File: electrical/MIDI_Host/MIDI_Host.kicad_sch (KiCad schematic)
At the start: 6 parts, among them CN1 USB-CON-AF-LCP-Offset, J1 Blackheadphonejack, J2 Blackheadphonejack, J3 USB_C_TYPE-C-32-M-12, SW1 ST-0-102-C03-N003-RS

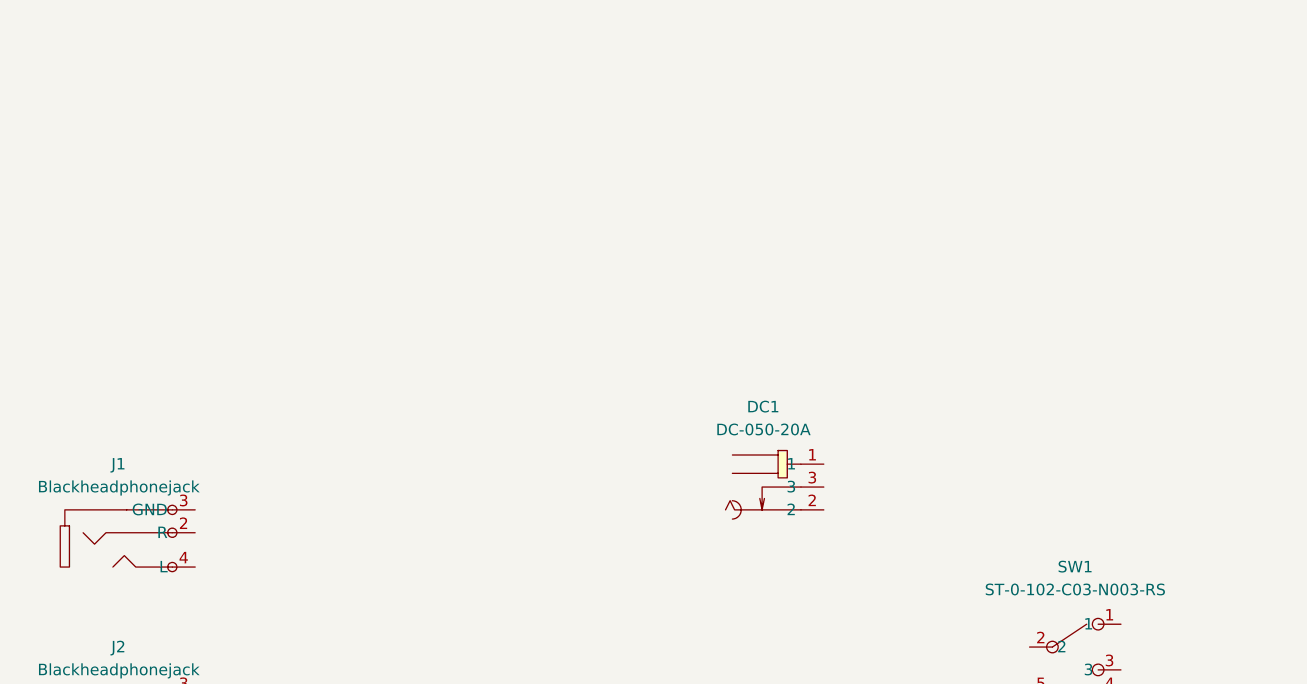
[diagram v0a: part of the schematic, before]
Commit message: SUKU host devboard created, cicd added
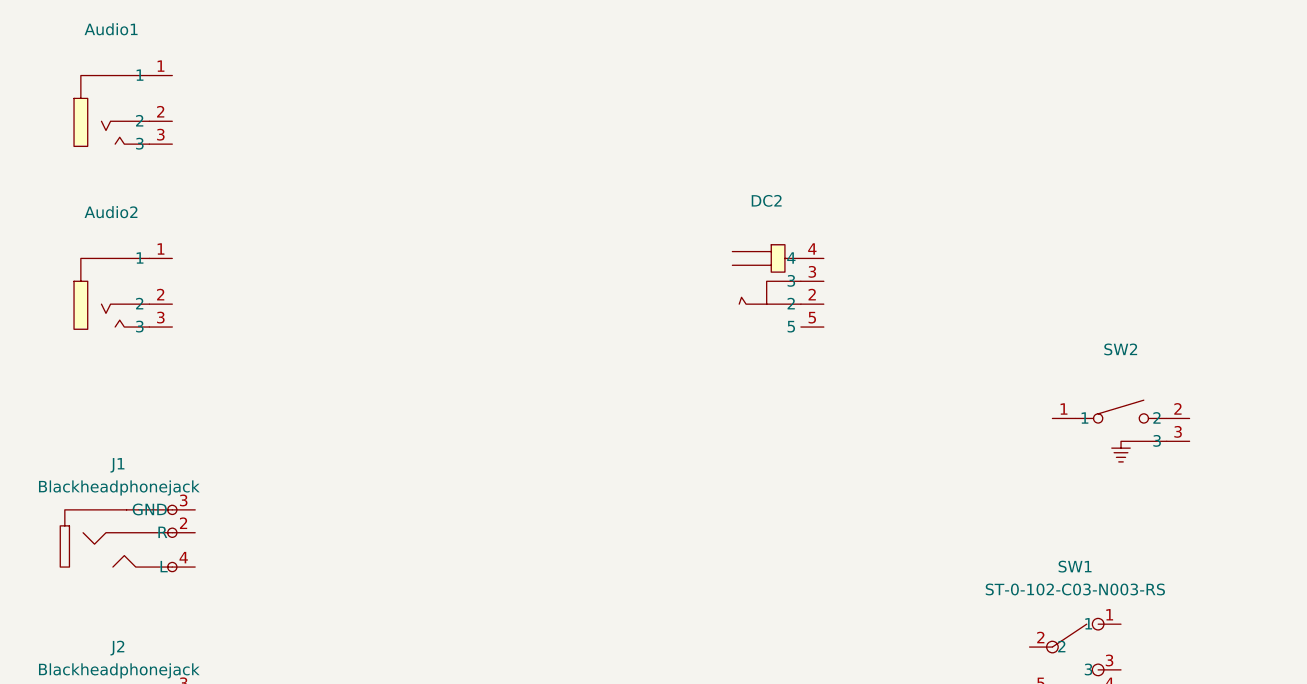
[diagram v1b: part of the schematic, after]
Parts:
- removed DC1: DC-050-20A, suku_basics:DC-IN-SMD_DC-050-20A, symbol suku_basics:DC-050-20A
- added Audio1, Audio2: (no value), symbol suku_basics:PJ-320B
- added DC2: (no value), symbol suku_basics:DC-C033D-5.5A-2.5
- added SW2: (no value), symbol suku_basics:TC-1109DE-C-G
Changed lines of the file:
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@@
     (pin "S4")
+  )
+  (symbol (lib_id "suku_basics:DC-C033D-5.5A-2.5") (at 139.7 38.1 0) (unit 1)
+    (in_bom yes) (on_board yes) (fields_autoplaced)
+    (property "Reference" "DC2" (id 0) (at 135.89 29.21 0))
+    (property "Value" "" (id 1) (at 135.89 31.75 0))
+    (property "Footprint" "" (id 2) (at 139.7 50.8 0)
+      (effects (font (size 1.27 1.27)) hide)
+    )
+    (property "Datasheet" "https://lcsc.com/product-detail/Power-Connectors_XKB-Enterprise-DC-C033D-5-5A-2-5_C397336.html" (id 3) (at 139.7 53.34 0)
+      (effects (font (size 1.27 1.27)) hide)
+    )
+    (property "Manufacturer" "XKB Enterprise" (id 4) (at 139.7 55.88 0)
+      (effects (font (size 1.27 1.27)) hide)
+    )
+    (property "LCSC Part" "C397336" (id 5) (at 139.7 58.42 0)
+      (effects (font (size 1.27 1.27)) hide)
+    )
+    (pin "2")
+    (pin "3")
+    (pin "4")
+    (pin "5")
   )
   (symbol (lib_id "suku_basics:Blackheadphonejack") (at 66.04 66.04 0) (unit 1)
@@
     (pin "5")
   )
+  (symbol (lib_id "suku_basics:PJ-320B") (at 66.04 38.1 0) (unit 1)
+    (in_bom yes) (on_board yes) (fields_autoplaced)
+    (property "Reference" "Audio2" (id 0) (at 63.12 30.48 0))
+    (property "Value" "" (id 1) (at 63.12 33.02 0))
+    (property "Footprint" "" (id 2) (at 66.04 50.8 0)
+      (effects (font (size 1.27 1.27)) hide)
+    )
+    (property "Datasheet" "https://lcsc.com/product-detail/Audio-Connectors_3-5mmCloth-headphone-jack_C18594.html" (id 3) (at 66.04 53.34 0)
+      (effects (font (size 1.27 1.27)) hide)
+    )
+    (property "Manufacturer" "BOOMELE" (id 4) (at 66.04 55.88 0)
+      (effects (font (size 1.27 1.27)) hide)
+    )
+    (property "LCSC Part" "C18594" (id 5) (at 66.04 58.42 0)
+      (effects (font (size 1.27 1.27)) hide)
+    )
+    (property "JLC Part" "Extended Part" (id 6) (at 66.04 60.96 0)
+      (effects (font (size 1.27 1.27)) hide)
+    )
+    (pin "1")
+    (pin "2")
+    (pin "3")
+  )
+  (symbol (lib_id "suku_basics:PJ-320B") (at 66.04 17.78 0) (unit 1)
+    (in_bom yes) (on_board yes) (fields_autoplaced)
+    (property "Reference" "Audio1" (id 0) (at 63.12 10.16 0))
+    (property "Value" "" (id 1) (at 63.12 12.7 0))
+    (property "Footprint" "" (id 2) (at 66.04 30.48 0)
+      (effects (font (size 1.27 1.27)) hide)
+    )
+    (property "Datasheet" "https://lcsc.com/product-detail/Audio-Connectors_3-5mmCloth-headphone-jack_C18594.html" (id 3) (at 66.04 33.02 0)
+      (effects (font (size 1.27 1.27)) hide)
+    )
+    (property "Manufacturer" "BOOMELE" (id 4) (at 66.04 35.56 0)
+      (effects (font (size 1.27 1.27)) hide)
+    )
+    (property "LCSC Part" "C18594" (id 5) (at 66.04 38.1 0)
+      (effects (font (size 1.27 1.27)) hide)
+    )
+    (property "JLC Part" "Extended Part" (id 6) (at 66.04 40.64 0)
+      (effects (font (size 1.27 1.27)) hide)
+    )
+    (pin "1")
+    (pin "2")
+    (pin "3")
+  )
+  (symbol (lib_id "suku_basics:TC-1109DE-C-G") (at 175.26 53.34 0) (unit 1)
+    (in_bom yes) (on_board yes) (fields_autoplaced)
+    (property "Reference" "SW2" (id 0) (at 175.26 45.72 0))
+    (property "Value" "" (id 1) (at 175.26 48.26 0))
+    (property "Footprint" "" (id 2) (at 175.26 63.5 0)
+      (effects (font (size 1.27 1.27)) hide)
+    )
+    (property "Datasheet" "https://lcsc.com/product-detail/Tactile-Switches_XKB-Enterprise-TC-1109DE-C-G_C400325.html" (id 3) (at 175.26 66.04 0)
+      (effects (font (size 1.27 1.27)) hide)
+    )
+    (property "Manufacturer" "XKB Enterprise" (id 4) (at 175.26 68.58 0)
+      (effects (font (size 1.27 1.27)) hide)
+    )
+    (property "LCSC Part" "C400325" (id 5) (at 175.26 71.12 0)
+      (effects (font (size 1.27 1.27)) hide)
+    )
+    (property "JLC Part" "Extended Part" (id 6) (at 175.26 73.66 0)
+      (effects (font (size 1.27 1.27)) hide)
+    )
+    (pin "1")
+    (pin "2")
+    (pin "3")
+  )
   (symbol (lib_id "suku_basics:Blackheadphonejack") (at 66.04 86.36 0) (unit 1)
     (in_bom yes) (on_board yes) (fields_autoplaced)
@@
     (pin "SH2")
   )
-  (symbol (lib_id "suku_basics:DC-050-20A") (at 139.7 60.96 0) (unit 1)
-    (in_bom yes) (on_board yes) (fields_autoplaced)
-    (property "Reference" "DC1" (id 0) (at 135.51 52.07 0))
-    (property "Value" "DC-050-20A" (id 1) (at 135.51 54.61 0))
-    (property "Footprint" "suku_basics:DC-IN-SMD_DC-050-20A" (id 2) (at 139.7 71.12 0)
-      (effects (font (size 1.27 1.27)) hide)
-    )
-    (property "Datasheet" "" (id 3) (at 139.7 60.96 0)
-      (effects (font (size 1.27 1.27)) hide)
-    )
-    (property "Manufacturer" "韩国韩荣" (id 4) (at 139.7 73.66 0)
-      (effects (font (size 1.27 1.27)) hide)
-    )
-    (property "LCSC Part" "C707276" (id 5) (at 139.7 76.2 0)
-      (effects (font (size 1.27 1.27)) hide)
-    )
-    (property "JLC Part" "Extended Part" (id 6) (at 139.7 78.74 0)
-      (effects (font (size 1.27 1.27)) hide)
-    )
-    (pin "1")
-    (pin "2")
-    (pin "3")
-  )
   (sheet_instances
     (path "/" (page "1"))
   )
   (symbol_instances
+    (path "/b58d647c-1ae7-4d06-97c8-66cde03fb16a"
+      (reference "Audio1") (unit 1) (value "PJ-320B") (footprint "suku_basics:AUDIO-SMD_PJ-320B")
+    )
+    (path "/a62f3716-14a3-419d-9103-6b6e5d48dea5"
+      (reference "Audio2") (unit 1) (value "PJ-320B") (footprint "suku_basics:AUDIO-SMD_PJ-320B")
+    )
     (path "/cc7fdda4-1f0b-4447-b8f5-2a7f9266383d"
       (reference "CN1") (unit 1) (value "USB-CON-AF-LCP-Offset") (footprint "suku_basics:USB-A-SMD_AF-LCP-OFFSET")
     )
-    (path "/da0518d1-a4a1-4d96-a115-d0b555fd0563"
-      (reference "DC1") (unit 1) (value "DC-050-20A") (footprint "suku_basics:DC-IN-SMD_DC-050-20A")
+    (path "/3ebfe238-c44b-4b15-bdba-ea713a53a98c"
+      (reference "DC2") (unit 1) (value "DC-C033D-5.5A-2.5") (footprint "suku_basics:DC-IN-TH_DC-C033D-5.5A-2.5")
     )
     (path "/450fd788-d806-48b1-a032-8afdc8273e6e"
@@
       (reference "SW1") (unit 1) (value "ST-0-102-C03-N003-RS") (footprint "suku_basics:SW-TH_ST-0-102-C03-N003-RS")
     )
-  )
+    (path "/be6da077-d179-463a-af26-1bac671e85bf"
+      (reference "SW2") (unit 1) (value "TC-1109DE-C-G") (footprint "suku_basics:SW-TH_3P-L4.5-W7.0-P3.00-LS1.9")
+    )
+  )

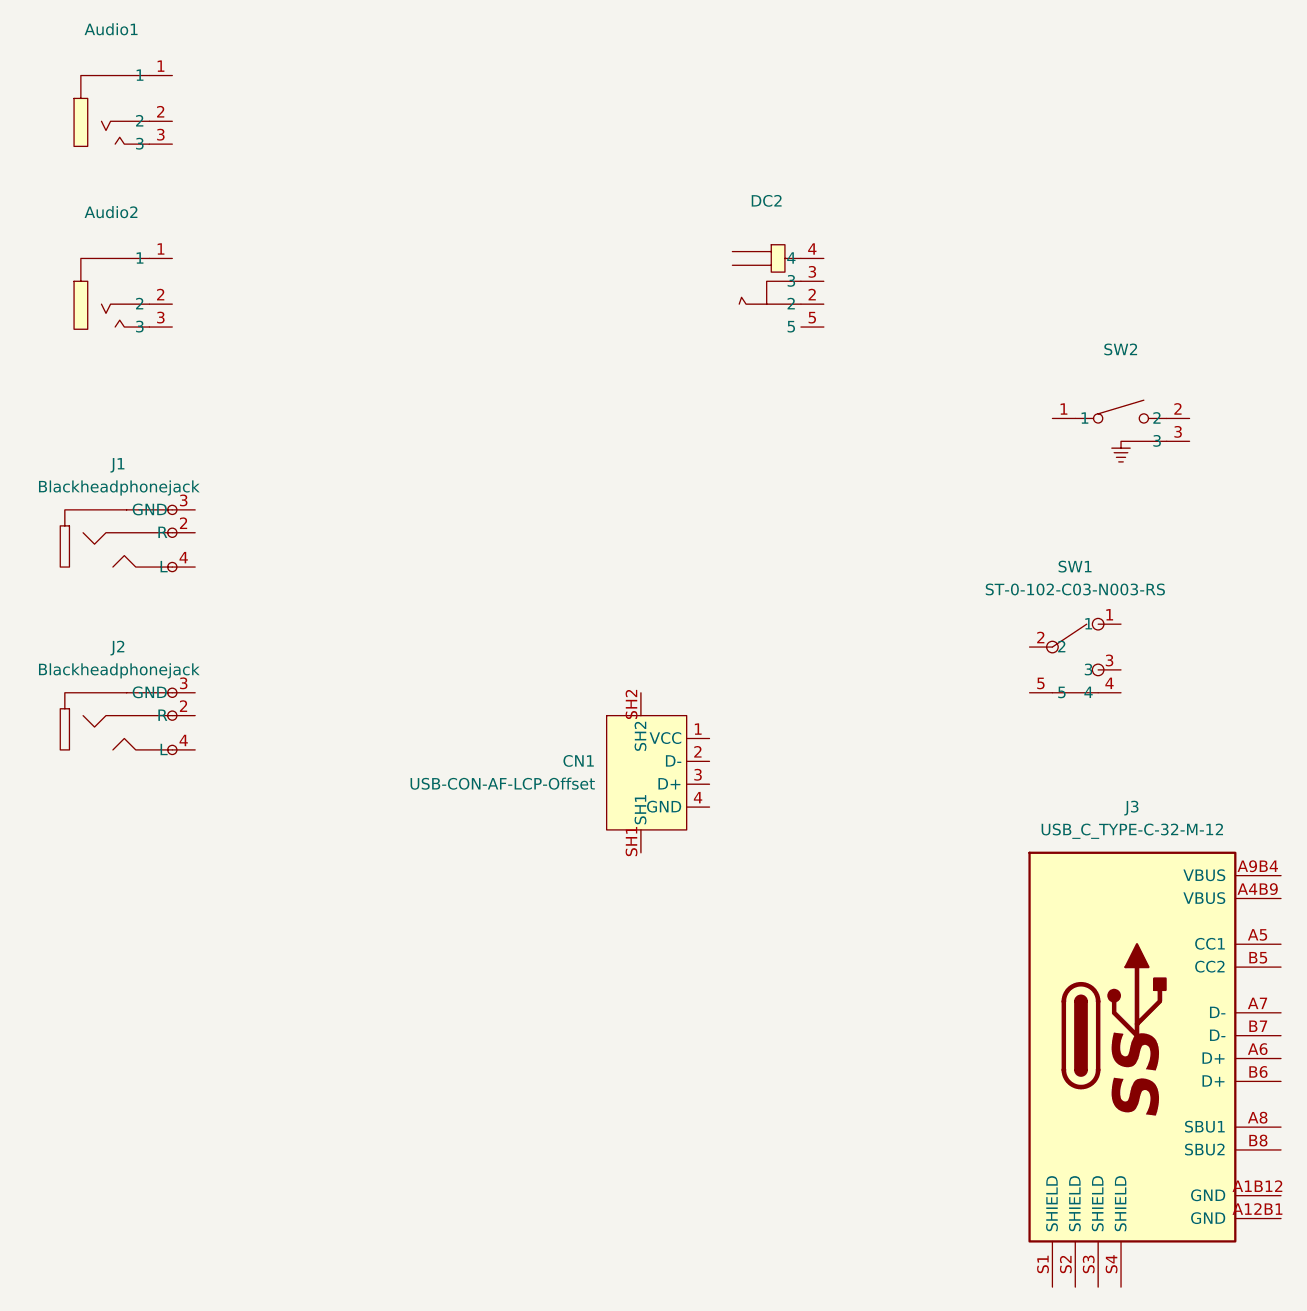
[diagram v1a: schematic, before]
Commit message: SUKU nc flags added to unused pins
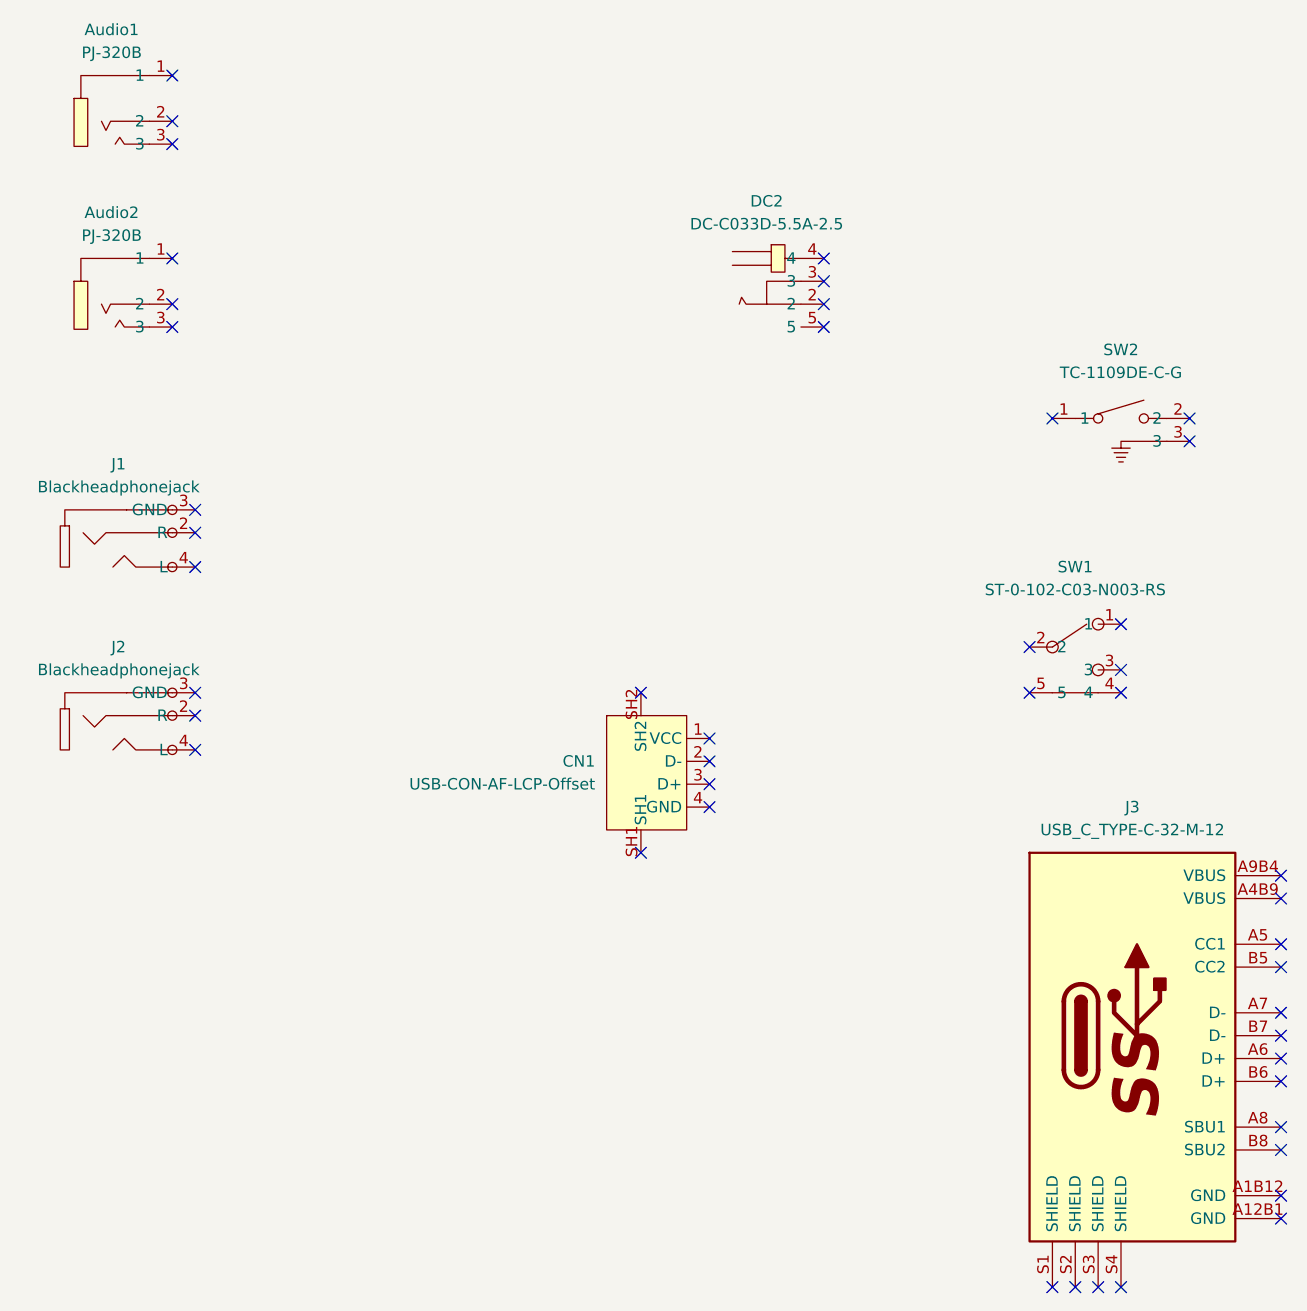
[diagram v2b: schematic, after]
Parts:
- Audio1, Audio2: value (none) -> PJ-320B; footprint (none) -> suku_basics:AUDIO-SMD_PJ-320B
- DC2: value (none) -> DC-C033D-5.5A-2.5; footprint (none) -> suku_basics:DC-IN-TH_DC-C033D-5.5A-2.5
- SW2: value (none) -> TC-1109DE-C-G; footprint (none) -> suku_basics:SW-TH_3P-L4.5-W7.0-P3.00-LS1.9
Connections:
- no-connect marks 0 -> 46
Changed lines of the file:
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@@
 (kicad_sch (version 20211123) (generator eeschema)
   (paper "A4")
+  (no_connect (at 142.24 35.56))
+  (no_connect (at 142.24 38.1))
+  (no_connect (at 142.24 40.64))
+  (no_connect (at 142.24 43.18))
+  (no_connect (at 72.39 83.82))
+  (no_connect (at 72.39 90.17))
+  (no_connect (at 72.39 86.36))
+  (no_connect (at 129.54 88.9))
+  (no_connect (at 129.54 91.44))
+  (no_connect (at 129.54 93.98))
+  (no_connect (at 121.92 101.6))
+  (no_connect (at 121.92 83.82))
+  (no_connect (at 129.54 96.52))
+  (no_connect (at 165.1 78.74))
+  (no_connect (at 165.1 83.82))
+  (no_connect (at 175.26 83.82))
+  (no_connect (at 193.04 104.14))
+  (no_connect (at 182.88 53.34))
+  (no_connect (at 182.88 55.88))
+  (no_connect (at 167.64 53.34))
+  (no_connect (at 175.26 81.28))
+  (no_connect (at 175.26 76.2))
+  (no_connect (at 167.64 149.86))
+  (no_connect (at 170.18 149.86))
+  (no_connect (at 172.72 149.86))
+  (no_connect (at 175.26 149.86))
+  (no_connect (at 193.04 142.24))
+  (no_connect (at 193.04 139.7))
+  (no_connect (at 193.04 134.62))
+  (no_connect (at 193.04 132.08))
+  (no_connect (at 193.04 127))
+  (no_connect (at 193.04 124.46))
+  (no_connect (at 193.04 121.92))
+  (no_connect (at 193.04 119.38))
+  (no_connect (at 193.04 114.3))
+  (no_connect (at 193.04 111.76))
+  (no_connect (at 193.04 106.68))
+  (no_connect (at 69.85 15.24))
+  (no_connect (at 69.85 20.32))
+  (no_connect (at 69.85 22.86))
+  (no_connect (at 69.85 40.64))
+  (no_connect (at 72.39 69.85))
+  (no_connect (at 72.39 66.04))
+  (no_connect (at 69.85 35.56))
+  (no_connect (at 69.85 43.18))
+  (no_connect (at 72.39 63.5))
   (symbol (lib_id "suku_basics:USB_C_TYPE-C-32-M-12") (at 177.8 121.92 0) (unit 1)
     (in_bom yes) (on_board yes) (fields_autoplaced)
@@
     (in_bom yes) (on_board yes) (fields_autoplaced)
     (property "Reference" "DC2" (id 0) (at 135.89 29.21 0))
-    (property "Value" "" (id 1) (at 135.89 31.75 0))
-    (property "Footprint" "" (id 2) (at 139.7 50.8 0)
+    (property "Value" "DC-C033D-5.5A-2.5" (id 1) (at 135.89 31.75 0))
+    (property "Footprint" "suku_basics:DC-IN-TH_DC-C033D-5.5A-2.5" (id 2) (at 139.7 50.8 0)
       (effects (font (size 1.27 1.27)) hide)
     )
@@
     (in_bom yes) (on_board yes) (fields_autoplaced)
     (property "Reference" "Audio2" (id 0) (at 63.12 30.48 0))
-    (property "Value" "" (id 1) (at 63.12 33.02 0))
-    (property "Footprint" "" (id 2) (at 66.04 50.8 0)
+    (property "Value" "PJ-320B" (id 1) (at 63.12 33.02 0))
+    (property "Footprint" "suku_basics:AUDIO-SMD_PJ-320B" (id 2) (at 66.04 50.8 0)
       (effects (font (size 1.27 1.27)) hide)
     )
@@
     (in_bom yes) (on_board yes) (fields_autoplaced)
     (property "Reference" "Audio1" (id 0) (at 63.12 10.16 0))
-    (property "Value" "" (id 1) (at 63.12 12.7 0))
-    (property "Footprint" "" (id 2) (at 66.04 30.48 0)
+    (property "Value" "PJ-320B" (id 1) (at 63.12 12.7 0))
+    (property "Footprint" "suku_basics:AUDIO-SMD_PJ-320B" (id 2) (at 66.04 30.48 0)
       (effects (font (size 1.27 1.27)) hide)
     )
@@
     (in_bom yes) (on_board yes) (fields_autoplaced)
     (property "Reference" "SW2" (id 0) (at 175.26 45.72 0))
-    (property "Value" "" (id 1) (at 175.26 48.26 0))
-    (property "Footprint" "" (id 2) (at 175.26 63.5 0)
+    (property "Value" "TC-1109DE-C-G" (id 1) (at 175.26 48.26 0))
+    (property "Footprint" "suku_basics:SW-TH_3P-L4.5-W7.0-P3.00-LS1.9" (id 2) (at 175.26 63.5 0)
       (effects (font (size 1.27 1.27)) hide)
     )

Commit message: SUKU schematic progress
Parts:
- removed Audio1, Audio2: PJ-320B, suku_basics:AUDIO-SMD_PJ-320B, symbol suku_basics:PJ-320B
- removed DC2: DC-C033D-5.5A-2.5, suku_basics:DC-IN-TH_DC-C033D-5.5A-2.5, symbol suku_basics:DC-C033D-5.5A-2.5
- removed J1, J2: Blackheadphonejack, suku_basics:AUDIO-TH_PJ-3200, symbol suku_basics:Blackheadphonejack
- removed J3: USB_C_TYPE-C-32-M-12, suku_basics:USB_C_Korean_Hroparts_TYPE-C-31-M-12, symbol suku_basics:USB_C_TYPE-C-32-M-12
- added U8: ESP32-WROOM-32U, RF_Module:ESP32-WROOM-32U, symbol RF_Module:ESP32-WROOM-32U
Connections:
- new net: U8.1 (GND), U8.15 (GND), U8.38 (GND), U8.39 (GND)
- no-connect marks 46 -> 17
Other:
- added sheet MIDI Frontened (midi.kicad_sch)
- added sheet Power Input (power.kicad_sch)
